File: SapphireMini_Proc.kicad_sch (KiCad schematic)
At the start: 39 parts, among them J801 USB_B_Micro, J802 Conn_02x05_Odd_Even, J803 Conn_02x05_Odd_Even, J805 Conn_01x04_Male, SW701 EVQP7C01P, SW801 EVQP7C01P, U801 ATSAMD21G18A-A

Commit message: Start of layout
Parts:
- removed L801: 10uH, SapphineMinimal:NR3012T100M, symbol Device:L
- C801, C810: footprint Capacitor_SMD:C_0603_1608Metric -> Capacitor_SMD:C_0402_1005Metric
- C802, C804: Voltage (none) -> 16
- C803: MPN CL10C391JB81PNC -> 06035A101JAT2A; Manufacturer (none) -> KYOCERA AVX
- C805, C808: footprint Capacitor_SMD:C_0603_1608Metric -> Capacitor_SMD:C_0805_2012Metric; Voltage (none) -> 16
- C806, C807, C809: footprint Capacitor_SMD:C_0603_1608Metric -> Capacitor_SMD:C_0402_1005Metric; Voltage (none) -> 25
- R809, R812, R813, R814: MPN (none) -> EXB-2HV470JV
- R810: MPN (none) -> RC0603JR-07330RL
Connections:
- net P3V3: now also C805.1, C806.1, C807.1, U801.17 (VDDIO), U801.36 (VDDIO), U801.44 (VDDIN)
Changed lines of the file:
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@@
   (junction (at 212.09 193.04) (diameter 0) (color 0 0 0 0)
   )
-  (junction (at 87.63 74.93) (diameter 0) (color 0 0 0 0)
-  )
   (junction (at 214.63 182.88) (diameter 0) (color 0 0 0 0)
   )
@@
     (stroke (width 0) (type default) (color 0 0 0 0))
   )
-  (wire (pts (xy 87.63 81.28) (xy 87.63 74.93))
+  (wire (pts (xy 87.63 71.12) (xy 87.63 81.28))
     (stroke (width 0) (type default) (color 0 0 0 0))
   )
@@
     (stroke (width 0) (type default) (color 0 0 0 0))
   )
-  (wire (pts (xy 87.63 48.26) (xy 87.63 43.18))
-    (stroke (width 0) (type default) (color 0 0 0 0))
-  )
   (wire (pts (xy 214.63 182.88) (xy 214.63 199.39))
     (stroke (width 0) (type default) (color 0 0 0 0))
@@
     (stroke (width 0) (type default) (color 0 0 0 0))
   )
-  (wire (pts (xy 87.63 74.93) (xy 87.63 71.12))
-    (stroke (width 0) (type default) (color 0 0 0 0))
-  )
   (wire (pts (xy 97.79 43.18) (xy 153.67 43.18))
     (stroke (width 0) (type default) (color 0 0 0 0))
@@
     (stroke (width 0) (type default) (color 0 0 0 0))
   )
-  (wire (pts (xy 87.63 55.88) (xy 87.63 57.15))
+  (wire (pts (xy 87.63 43.18) (xy 87.63 57.15))
     (stroke (width 0) (type default) (color 0 0 0 0))
   )
@@
     (effects (font (size 1.27 1.27)) (justify right))
   )
-  (hierarchical_label "RESET" (shape input) (at 24.13 190.5 180)
-    (effects (font (size 1.27 1.27)) (justify right))
-  )
   (hierarchical_label "LOCAL_PPS" (shape input) (at 344.17 190.5 180)
     (effects (font (size 1.27 1.27)) (justify right))
@@
     (effects (font (size 1.27 1.27)) (justify right))
   )
-  (hierarchical_label "SD_CD" (shape input) (at 344.17 80.01 180)
+  (hierarchical_label "SD_CD" (shape input) (at 345.44 80.01 180)
     (effects (font (size 1.27 1.27)) (justify right))
   )
@@
       (effects (font (size 1.27 1.27)) hide)
     )
+    (property "Voltage" "16" (id 8) (at 66.04 93.98 0)
+      (effects (font (size 1.27 1.27)) hide)
+    )
     (pin "1")
     (pin "2")
@@
     (property "Reference" "C809" (id 0) (at 109.22 64.7192 90))
     (property "Value" "100nF" (id 1) (at 109.22 67.0306 90))
-    (property "Footprint" "Capacitor_SMD:C_0603_1608Metric" (id 2) (at 105.41 72.0852 0)
+    (property "Footprint" "Capacitor_SMD:C_0402_1005Metric" (id 2) (at 105.41 72.0852 0)
       (effects (font (size 1.27 1.27)) hide)
     )
@@
       (effects (font (size 1.27 1.27)) hide)
     )
+    (property "Voltage" "25" (id 8) (at 109.22 71.12 0)
+      (effects (font (size 1.27 1.27)) hide)
+    )
     (pin "1")
     (pin "2")
@@
     (property "Reference" "C808" (id 0) (at 109.22 52.0192 90))
     (property "Value" "22uF" (id 1) (at 109.22 54.3306 90))
-    (property "Footprint" "Capacitor_SMD:C_0603_1608Metric" (id 2) (at 105.41 59.3852 0)
+    (property "Footprint" "Capacitor_SMD:C_0805_2012Metric" (id 2) (at 105.41 59.3852 0)
       (effects (font (size 1.27 1.27)) hide)
     )
@@
       (effects (font (size 1.27 1.27)) hide)
     )
+    (property "Voltage" "16" (id 8) (at 109.22 58.42 0)
+      (effects (font (size 1.27 1.27)) hide)
+    )
     (pin "1")
     (pin "2")
@@
     (property "Reference" "C806" (id 0) (at 83.82 64.7192 90))
     (property "Value" "100nF" (id 1) (at 83.82 67.0306 90))
-    (property "Footprint" "Capacitor_SMD:C_0603_1608Metric" (id 2) (at 80.01 72.0852 0)
+    (property "Footprint" "Capacitor_SMD:C_0402_1005Metric" (id 2) (at 80.01 72.0852 0)
       (effects (font (size 1.27 1.27)) hide)
     )
@@
       (effects (font (size 1.27 1.27)) hide)
     )
+    (property "Voltage" "25" (id 8) (at 83.82 71.12 0)
+      (effects (font (size 1.27 1.27)) hide)
+    )
     (pin "1")
     (pin "2")
@@
     (property "Reference" "C807" (id 0) (at 83.82 74.8792 90))
     (property "Value" "100nF" (id 1) (at 83.82 77.1906 90))
-    (property "Footprint" "Capacitor_SMD:C_0603_1608Metric" (id 2) (at 80.01 82.2452 0)
+    (property "Footprint" "Capacitor_SMD:C_0402_1005Metric" (id 2) (at 80.01 82.2452 0)
       (effects (font (size 1.27 1.27)) hide)
     )
@@
       (effects (font (size 1.27 1.27)) hide)
     )
+    (property "Voltage" "25" (id 8) (at 83.82 81.28 0)
+      (effects (font (size 1.27 1.27)) hide)
+    )
     (pin "1")
     (pin "2")
@@
       (effects (font (size 1.27 1.27)) hide)
     )
+    (property "Description" "2 kOhms ±1% 0.1W, 1/10W Chip Resistor 0603" (id 6) (at 49.53 196.85 0)
+      (effects (font (size 1.27 1.27)) hide)
+    )
     (pin "1")
     (pin "2")
@@
       (effects (font (size 1.27 1.27)) hide)
     )
-    (property "Description" "390 pF ±5% 50V Ceramic Capacitor C0G, NP0 0603" (id 4) (at 59.69 196.85 0)
+    (property "Description" "100 pF ±5% 50V Ceramic Capacitor C0G, NP0 0603 (1608 Metric)" (id 4) (at 59.69 196.85 0)
       (effects (font (size 1.27 1.27)) hide)
     )
-    (property "MPN" "CL10C391JB81PNC" (id 5) (at 59.69 196.85 0)
+    (property "MPN" "06035A101JAT2A" (id 5) (at 59.69 196.85 0)
+      (effects (font (size 1.27 1.27)) hide)
+    )
+    (property "Manufacturer" "KYOCERA AVX" (id 6) (at 59.69 196.85 0)
       (effects (font (size 1.27 1.27)) hide)
     )
@@
       (effects (font (size 1.27 1.27)) hide)
     )
+    (property "Description" "330 Ohms ±5% 0.1W, 1/10W Chip Resistor 0603 (1608 Metric) Moisture Resistant Thick Film" (id 4) (at 40.64 190.5 0)
+      (effects (font (size 1.27 1.27)) hide)
+    )
+    (property "MPN" "RC0603JR-07330RL" (id 5) (at 40.64 190.5 0)
+      (effects (font (size 1.27 1.27)) hide)
+    )
     (pin "1")
     (pin "2")
@@
       (effects (font (size 1.27 1.27)) hide)
     )
+    (property "Description" "2 kOhms ±1% 0.1W, 1/10W Chip Resistor 0603" (id 6) (at 217.17 87.63 0)
+      (effects (font (size 1.27 1.27)) hide)
+    )
     (pin "1")
     (pin "2")
@@
       (effects (font (size 1.27 1.27)) hide)
     )
+    (property "Voltage" "16" (id 8) (at 49.53 114.3 0)
+      (effects (font (size 1.27 1.27)) hide)
+    )
     (pin "1")
     (pin "2")
@@
       (effects (font (size 1.27 1.27)) (justify left))
     )
-    (property "Footprint" "Capacitor_SMD:C_0603_1608Metric" (id 2) (at 194.31 213.36 0)
+    (property "Footprint" "Capacitor_SMD:C_0402_1005Metric" (id 2) (at 194.31 213.36 0)
       (effects (font (size 1.27 1.27)) hide)
     )
@@
       (effects (font (size 1.27 1.27)) (justify left))
     )
-    (property "Footprint" "Capacitor_SMD:C_0603_1608Metric" (id 2) (at 191.77 88.9 0)
+    (property "Footprint" "Capacitor_SMD:C_0402_1005Metric" (id 2) (at 191.77 88.9 0)
       (effects (font (size 1.27 1.27)) hide)
     )
@@
     (pin "9")
   )
-  (symbol (lib_id "power:PWR_FLAG") (at 87.63 74.93 270) (unit 1)
-    (in_bom yes) (on_board yes)
-    (property "Reference" "#FLG0801" (id 0) (at 89.535 74.93 0)
-      (effects (font (size 1.27 1.27)) hide)
-    )
-    (property "Value" "PWR_FLAG" (id 1) (at 90.8049 74.4962 0)
-      (effects (font (size 1.27 1.27)) (justify left))
-    )
-    (property "Footprint" "" (id 2) (at 87.63 74.93 0)
-      (effects (font (size 1.27 1.27)) hide)
-    )
-    (property "Datasheet" "~" (id 3) (at 87.63 74.93 0)
-      (effects (font (size 1.27 1.27)) hide)
-    )
-    (pin "1")
-  )
-  (symbol (lib_id "Device:L") (at 87.63 52.07 0) (unit 1)
-    (in_bom yes) (on_board yes)
-    (property "Reference" "L801" (id 0) (at 88.9 50.8 0)
-      (effects (font (size 1.27 1.27)) (justify left))
-    )
-    (property "Value" "10uH" (id 1) (at 88.9 53.34 0)
-      (effects (font (size 1.27 1.27)) (justify left))
-    )
-    (property "Footprint" "SapphineMinimal:NR3012T100M" (id 2) (at 87.63 52.07 0)
-      (effects (font (size 1.27 1.27)) hide)
-    )
-    (property "Datasheet" "~" (id 3) (at 87.63 52.07 0)
-      (effects (font (size 1.27 1.27)) hide)
-    )
-    (property "Description" "FIXED IND 10UH 630MA 348MOHM SMD" (id 4) (at 87.63 52.07 0)
-      (effects (font (size 1.27 1.27)) hide)
-    )
-    (property "MPN" "NR3012T100M" (id 5) (at 87.63 52.07 0)
-      (effects (font (size 1.27 1.27)) hide)
-    )
-    (property "Manufacturer" "Taiyo Yuden" (id 6) (at 87.63 52.07 0)
-      (effects (font (size 1.27 1.27)) hide)
-    )
-    (pin "1")
-    (pin "2")
-  )
   (symbol (lib_id "Device:C") (at 83.82 57.15 270) (unit 1)
     (in_bom yes) (on_board yes)
     (property "Reference" "C805" (id 0) (at 83.82 50.7492 90))
     (property "Value" "22uF" (id 1) (at 83.82 53.0606 90))
-    (property "Footprint" "Capacitor_SMD:C_0603_1608Metric" (id 2) (at 80.01 58.1152 0)
+    (property "Footprint" "Capacitor_SMD:C_0805_2012Metric" (id 2) (at 80.01 58.1152 0)
       (effects (font (size 1.27 1.27)) hide)
     )
@@
       (effects (font (size 1.27 1.27)) hide)
     )
+    (property "Voltage" "16" (id 8) (at 83.82 57.15 0)
+      (effects (font (size 1.27 1.27)) hide)
+    )
     (pin "1")
     (pin "2")
@@
       (effects (font (size 1.524 1.524)))
     )
+    (property "MPN" "EXB-2HV470JV" (id 4) (at 355.6 127 0)
+      (effects (font (size 1.27 1.27)) hide)
+    )
     (pin "1")
     (pin "10")
@@
       (effects (font (size 1.524 1.524)))
     )
+    (property "MPN" "EXB-2HV470JV" (id 4) (at 355.6 80.01 0)
+      (effects (font (size 1.27 1.27)) hide)
+    )
     (pin "1")
     (pin "10")
@@
       (effects (font (size 1.524 1.524)))
     )
+    (property "MPN" "EXB-2HV470JV" (id 4) (at 355.6 175.26 0)
+      (effects (font (size 1.27 1.27)) hide)
+    )
     (pin "1")
     (pin "10")
@@
       (effects (font (size 1.524 1.524)))
     )
+    (property "MPN" "EXB-2HV470JV" (id 4) (at 356.87 31.75 0)
+      (effects (font (size 1.27 1.27)) hide)
+    )
     (pin "1")

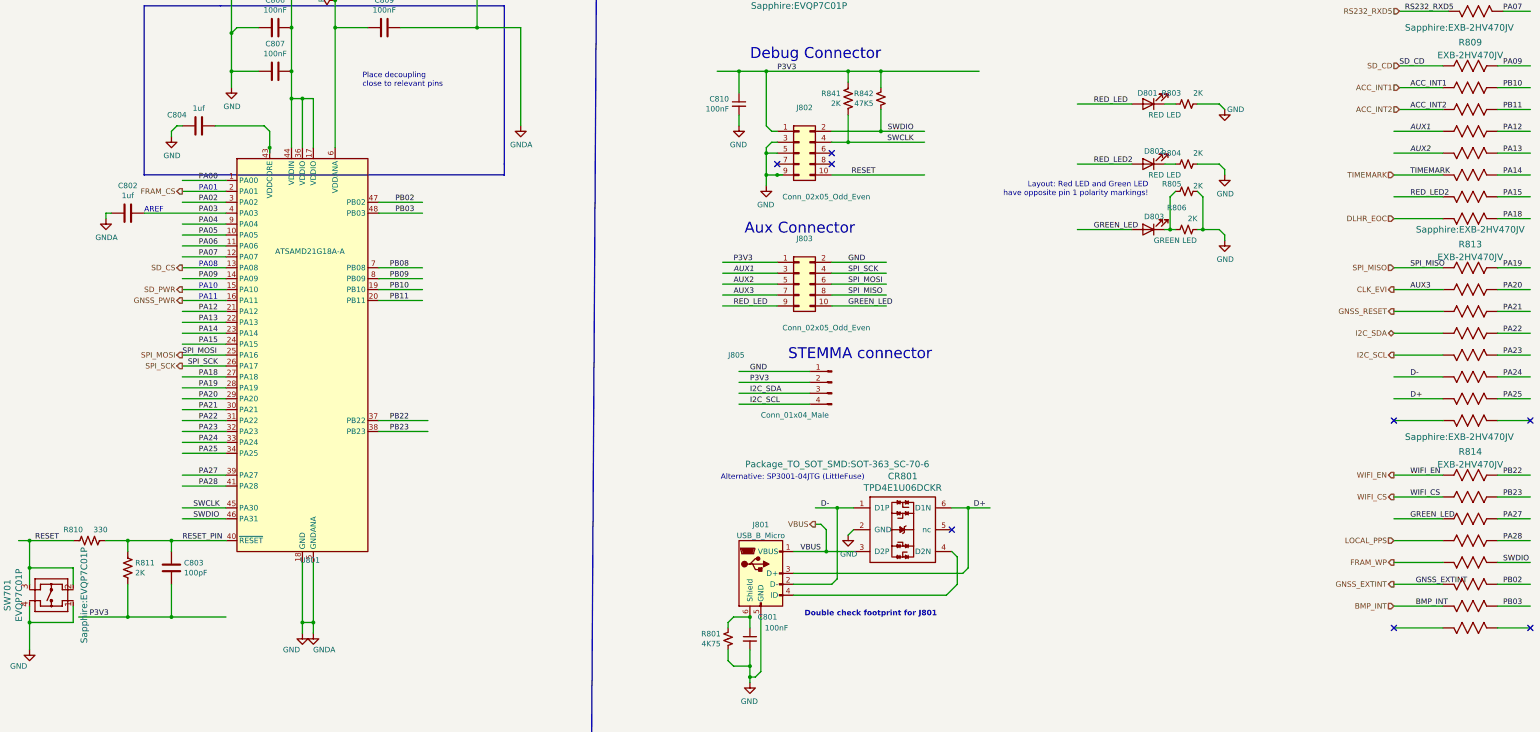
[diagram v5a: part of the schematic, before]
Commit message: updated new layout - no routing
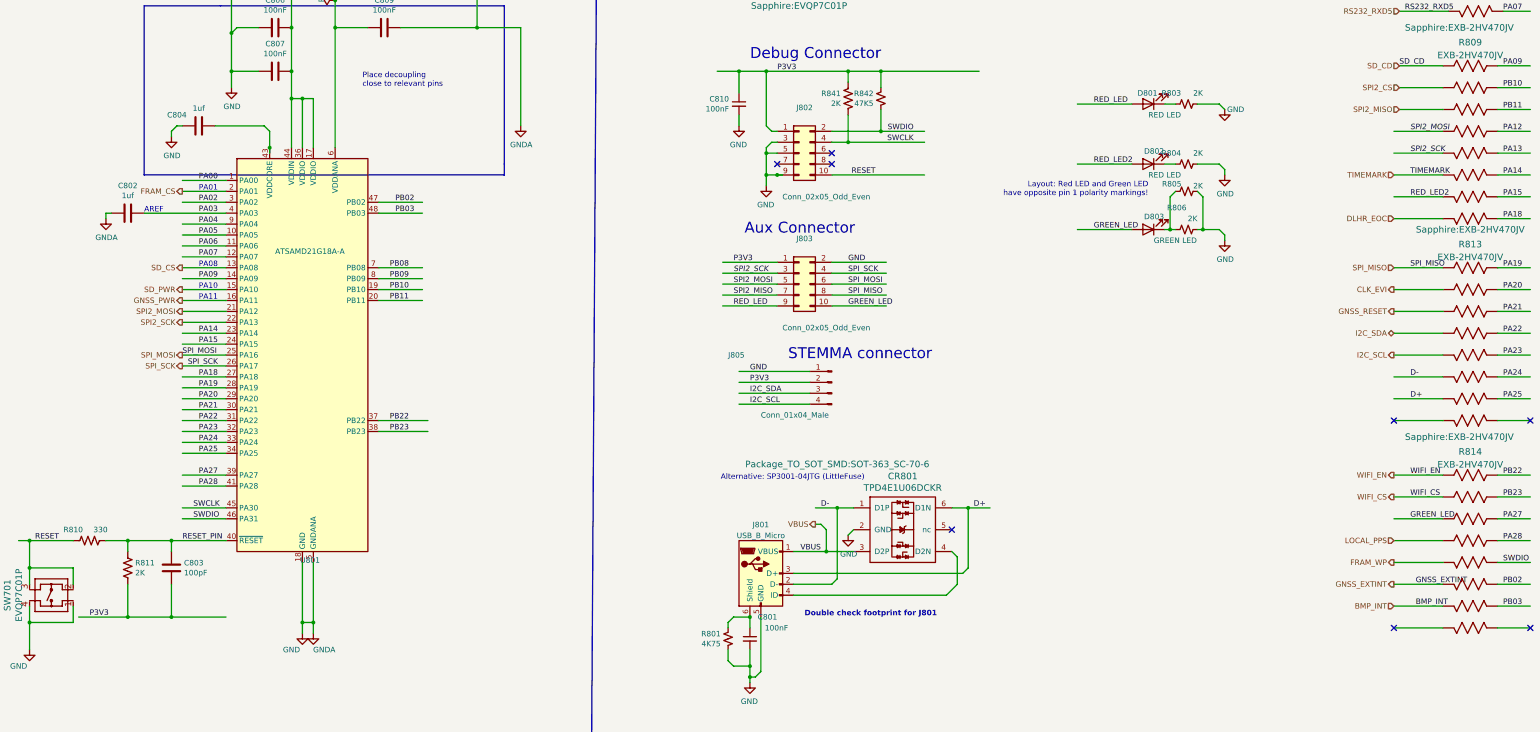
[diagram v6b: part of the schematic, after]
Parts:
- R809, R812, R813, R814: symbol PanasonicRA:EXB-2HV470JV -> sapphireMini:EXB-2HV470JV_1
- SW701, SW801: symbol EVQP7C01P:EVQP7C01P -> sapphireMini:EVQP7C01P
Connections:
- net CLK_EVI: no longer J803.7 (Pin_7)
- net PA12: no longer U801.21 (PA12)
- net PA13: no longer U801.22 (PA13)
- net ACC_INT1 renamed SPI2_CS
- net ACC_INT2 renamed SPI2_MISO
- net SPI2_MISO: now also J803.7 (Pin_7)
- net AUX1 renamed SPI2_MOSI
- net SPI2_MOSI: now also J803.5 (Pin_5), U801.21 (PA12); no longer J803.3 (Pin_3)
- net AUX2 renamed SPI2_SCK
- net SPI2_SCK: now also J803.3 (Pin_3), U801.22 (PA13); no longer J803.5 (Pin_5)
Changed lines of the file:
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@@
-    (effects (font (size 1.27 1.27)) (justify left bottom))
-  )
-  (label "ACC_INT2" (at 347.98 90.17 0)
     (effects (font (size 1.27 1.27)) (justify left bottom))
   )
@@
     (effects (font (size 1.27 1.27)) (justify left bottom))
   )
-  (label "ACC_INT1" (at 347.98 85.09 0)
-    (effects (font (size 1.27 1.27)) (justify left bottom))
-  )
   (label "PB02" (at 111.76 111.76 0)
     (effects (font (size 1.27 1.27)) (justify left bottom))
   )
-  (label "AUX1" (at 347.98 95.25 0)
+  (label "SPI2_MOSI" (at 347.98 95.25 0)
     (effects (font (size 1.27 1.27) italic) (justify left bottom))
   )
@@
     (effects (font (size 1.27 1.27)) (justify left bottom))
   )
-  (label "AUX2" (at 190.5 130.81 0)
+  (label "SPI2_MOSI" (at 190.5 130.81 0)
     (effects (font (size 1.27 1.27)) (justify left bottom))
   )
@@
     (effects (font (size 1.27 1.27)) (justify left bottom))
   )
-  (label "AUX1" (at 190.5 128.27 0)
+  (label "SPI2_SCK" (at 190.5 128.27 0)
     (effects (font (size 1.27 1.27) italic) (justify left bottom))
   )
@@
     (effects (font (size 1.27 1.27)) (justify left bottom))
   )
-  (label "AUX3" (at 190.5 133.35 0)
+  (label "SPI2_MISO" (at 190.5 133.35 0)
     (effects (font (size 1.27 1.27)) (justify left bottom))
   )
@@
     (effects (font (size 1.27 1.27)) (justify left bottom))
   )
-  (label "PA12" (at 66.04 137.16 0)
-    (effects (font (size 1.27 1.27)) (justify left bottom))
-  )
   (label "PA07" (at 66.04 124.46 0)
     (effects (font (size 1.27 1.27)) (justify left bottom))
@@
   )
   (label "GND" (at 194.31 151.13 0)
-    (effects (font (size 1.27 1.27)) (justify left bottom))
-  )
-  (label "PA13" (at 66.04 139.7 0)
     (effects (font (size 1.27 1.27)) (justify left bottom))
   )
@@
     (effects (font (size 1.27 1.27)) (justify left bottom))
   )
-  (label "AUX3" (at 347.98 132.08 0)
-    (effects (font (size 1.27 1.27)) (justify left bottom))
-  )
-  (label "AUX2" (at 347.98 100.33 0)
+  (label "SPI2_SCK" (at 347.98 100.33 0)
     (effects (font (size 1.27 1.27) italic) (justify left bottom))
   )
@@
     (effects (font (size 1.27 1.27)) (justify right))
   )
+  (hierarchical_label "SPI2_CS" (shape input) (at 345.44 85.09 180)
+    (effects (font (size 1.27 1.27)) (justify right))
+  )
   (hierarchical_label "SD_PWR" (shape output) (at 62.23 132.08 180)
     (effects (font (size 1.27 1.27)) (justify right))
   )
-  (hierarchical_label "ACC_INT1" (shape input) (at 345.44 85.09 180)
-    (effects (font (size 1.27 1.27)) (justify right))
-  )
   (hierarchical_label "WIFI_IRQ" (shape input) (at 345.44 46.99 180)
     (effects (font (size 1.27 1.27)) (justify right))
@@
     (effects (font (size 1.27 1.27)) (justify right))
   )
-  (hierarchical_label "ACC_INT2" (shape input) (at 345.44 90.17 180)
-    (effects (font (size 1.27 1.27)) (justify right))
-  )
   (hierarchical_label "LOCAL_PPS" (shape input) (at 344.17 190.5 180)
     (effects (font (size 1.27 1.27)) (justify right))
@@
     (effects (font (size 1.27 1.27)) (justify right))
   )
+  (hierarchical_label "SPI2_SCK" (shape output) (at 62.23 139.7 180)
+    (effects (font (size 1.27 1.27)) (justify right))
+  )
   (hierarchical_label "SD_CS" (shape output) (at 62.23 127 180)
     (effects (font (size 1.27 1.27)) (justify right))
@@
     (effects (font (size 1.27 1.27)) (justify right))
   )
+  (hierarchical_label "SPI2_MISO" (shape input) (at 345.44 90.17 180)
+    (effects (font (size 1.27 1.27)) (justify right))
+  )
   (hierarchical_label "I2C_SDA" (shape bidirectional) (at 344.17 142.24 180)
+    (effects (font (size 1.27 1.27)) (justify right))
+  )
+  (hierarchical_label "SPI2_MOSI" (shape output) (at 62.23 137.16 180)
     (effects (font (size 1.27 1.27)) (justify right))
   )
@@
     (pin "2")
   )
-  (symbol (lib_id "EVQP7C01P:EVQP7C01P") (at 179.07 59.69 0) (unit 1)
+  (symbol (lib_id "sapphireMini:EVQP7C01P") (at 179.07 59.69 0) (unit 1)
     (in_bom yes) (on_board yes)
     (property "Reference" "SW801" (id 0) (at 205.74 48.1838 0)
@@
     (pin "4")
   )
-  (symbol (lib_id "EVQP7C01P:EVQP7C01P") (at 33.02 229.87 90) (unit 1)
+  (symbol (lib_name "EVQP7C01P_1") (lib_id "sapphireMini:EVQP7C01P") (at 33.02 229.87 90) (unit 1)
     (in_bom yes) (on_board yes)
     (property "Reference" "SW701" (id 0) (at 21.5138 203.2 0)
@@
       (effects (font (size 1.524 1.524)))
     )
-    (property "Footprint" "Sapphire:EVQP7C01P" (id 2) (at 39.37 203.2 0)
-      (effects (font (size 1.524 1.524)))
+    (property "Footprint" "Sapphire:EVQP7C01P" (id 2) (at 27.305 186.055 90)
+      (effects (font (size 1.524 1.524)) hide)
     )
     (property "Datasheet" "" (id 3) (at 33.02 229.87 0)
@@
     (pin "4")
   )
-  (symbol (lib_id "PanasonicRA:EXB-2HV470JV") (at 355.6 127 0) (unit 1)
+  (symbol (lib_id "sapphireMini:EXB-2HV470JV_1") (at 355.6 127 0) (unit 1)
     (in_bom yes) (on_board yes)
     (property "Reference" "R813" (id 0) (at 361.95 121.5443 0)
@@
     (pin "6")
   )
-  (symbol (lib_id "PanasonicRA:EXB-2HV470JV") (at 355.6 80.01 0) (unit 1)
+  (symbol (lib_id "sapphireMini:EXB-2HV470JV_1") (at 355.6 80.01 0) (unit 1)
     (in_bom yes) (on_board yes)
     (property "Reference" "R809" (id 0) (at 361.95 74.5543 0)
@@
     (pin "9")
   )
-  (symbol (lib_id "PanasonicRA:EXB-2HV470JV") (at 355.6 175.26 0) (unit 1)
+  (symbol (lib_id "sapphireMini:EXB-2HV470JV_1") (at 355.6 175.26 0) (unit 1)
     (in_bom yes) (on_board yes)
     (property "Reference" "R814" (id 0) (at 361.95 169.8043 0)
@@
     (pin "2")
   )
-  (symbol (lib_id "PanasonicRA:EXB-2HV470JV") (at 356.87 31.75 0) (unit 1)
+  (symbol (lib_id "sapphireMini:EXB-2HV470JV_1") (at 356.87 31.75 0) (unit 1)
     (in_bom yes) (on_board yes)
     (property "Reference" "R812" (id 0) (at 363.22 26.2943 0)
